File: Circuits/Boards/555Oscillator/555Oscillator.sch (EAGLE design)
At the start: 8 parts

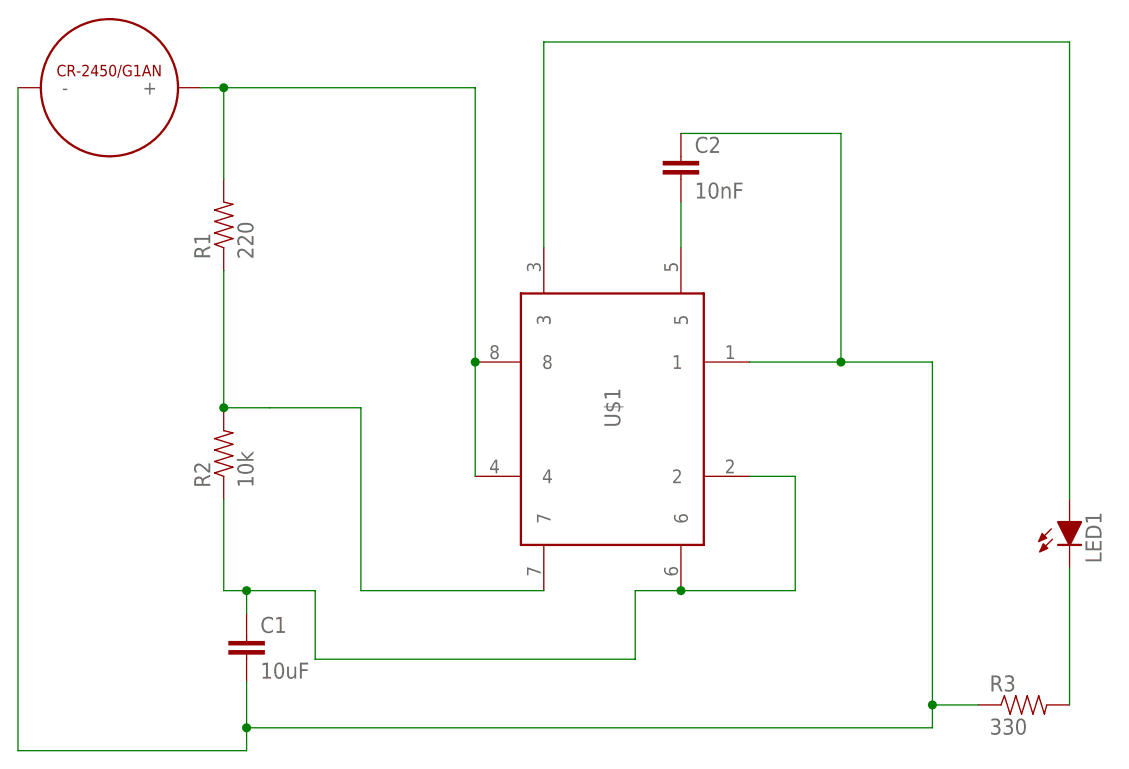
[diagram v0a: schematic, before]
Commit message: updated 555 board
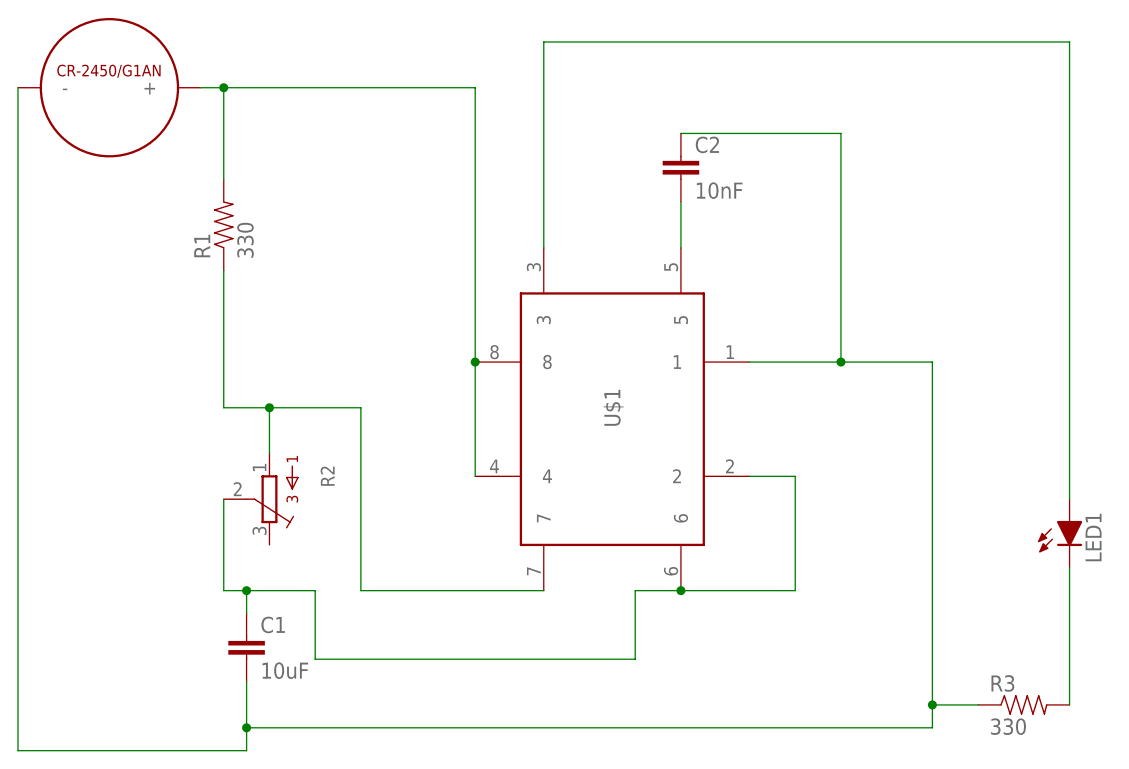
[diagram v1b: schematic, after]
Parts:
- R1: value 220 -> 330
- R2: value 10k -> (none); device HyTechDevices:RESISTORAXIAL-0.3 -> HyTechDevices:TRIMPOT_3296C
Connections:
- net N$13: now also R2.2; no longer R2.1
- net N$3: now also R2.1; no longer R2.2
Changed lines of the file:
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@@
 <?xml version="1.0" encoding="utf-8"?>
 <!DOCTYPE eagle SYSTEM "eagle.dtd">
-<eagle version="9.1.3">
+<eagle version="9.4.2">
 <drawing>
 <settings>
@@
 <part name="C1" library="HyTechDevices" deviceset="CAP" device="_" value="10uF"/>
 <part name="C2" library="HyTechDevices" deviceset="CAP" device="_" value="10nF"/>
-<part name="R1" library="HyTechDevices" deviceset="RESISTOR" device="AXIAL-0.3" value="220"/>
+<part name="R1" library="HyTechDevices" deviceset="RESISTOR" device="AXIAL-0.3" value="330"/>
+<part name="R2" library="HyTechDevices" deviceset="TRIMPOT_3296" device="C"/>
 <part name="LED1" library="HyTechDevices" deviceset="LED" device="-5MM"/>
 <part name="R3" library="HyTechDevices" deviceset="RESISTOR" device="AXIAL-0.3" value="330"/>
-<part name="R2" library="HyTechDevices" deviceset="RESISTOR" device="AXIAL-0.3" value="10k"/>
 </parts>
 <sheets>
@@
 <attribute name="VALUE" x="8.382" y="74.93" size="1.778" layer="96" rot="R90"/>
 </instance>
+<instance part="R2" gate="G$1" x="10.16" y="48.26" smashed="yes" rot="R180">
+<attribute name="NAME" x="15.875" y="52.07" size="1.524" layer="95" ratio="10" rot="R270"/>
+<attribute name="VALUE" x="13.97" y="52.07" size="1.524" layer="96" ratio="10" rot="R270"/>
+</instance>
 <instance part="LED1" gate="LED" x="99.06" y="45.72" smashed="yes">
 <attribute name="NAME" x="102.616" y="41.148" size="1.778" layer="95" rot="R90"/>
@@
 <attribute name="NAME" x="90.17" y="26.8986" size="1.778" layer="95"/>
 <attribute name="VALUE" x="90.17" y="22.098" size="1.778" layer="96"/>
-</instance>
-<instance part="R2" gate="G$1" x="5.08" y="53.34" smashed="yes" rot="R90">
-<attribute name="NAME" x="3.5814" y="49.53" size="1.778" layer="95" rot="R90"/>
-<attribute name="VALUE" x="8.382" y="49.53" size="1.778" layer="96" rot="R90"/>
 </instance>
 </instances>
@@
 <wire x1="20.32" y1="38.1" x2="20.32" y2="58.42" width="0.1524" layer="91"/>
 <wire x1="20.32" y1="58.42" x2="10.16" y2="58.42" width="0.1524" layer="91"/>
+<pinref part="R2" gate="G$1" pin="1"/>
+<wire x1="10.16" y1="58.42" x2="10.16" y2="53.34" width="0.1524" layer="91"/>
+<junction x="10.16" y="58.42"/>
 <pinref part="R1" gate="G$1" pin="1"/>
 <wire x1="10.16" y1="58.42" x2="5.08" y2="58.42" width="0.1524" layer="91"/>
 <wire x1="5.08" y1="58.42" x2="5.08" y2="73.66" width="0.1524" layer="91"/>
-<pinref part="R2" gate="G$1" pin="2"/>
-<junction x="5.08" y="58.42"/>
 </segment>
 </net>
@@
 <wire x1="7.62" y1="38.1" x2="7.62" y2="35.56" width="0.1524" layer="91"/>
 <wire x1="15.24" y1="38.1" x2="7.62" y2="38.1" width="0.1524" layer="91"/>
+<pinref part="R2" gate="G$1" pin="2"/>
+<wire x1="5.08" y1="48.26" x2="5.08" y2="38.1" width="0.1524" layer="91"/>
 <wire x1="5.08" y1="38.1" x2="7.62" y2="38.1" width="0.1524" layer="91"/>
 <junction x="7.62" y="38.1"/>
-<pinref part="R2" gate="G$1" pin="1"/>
-<wire x1="5.08" y1="38.1" x2="5.08" y2="48.26" width="0.1524" layer="91"/>
-</segment>
-</net>
+</segment>
+</net>
